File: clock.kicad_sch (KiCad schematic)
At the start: 31 parts, among them J1 USB_C_Receptacle_USB2.0_16P, J2 Conn_01x02_Pin, J3 Conn_01x02_Pin, J4 Conn_01x02_Pin, SW1 SW_Push, SW2 SW_Push, SW3 SW_Push, U1 STM32F072CBT6, U2 USBLC6-2SC6, U3 AZ1117C-3.3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

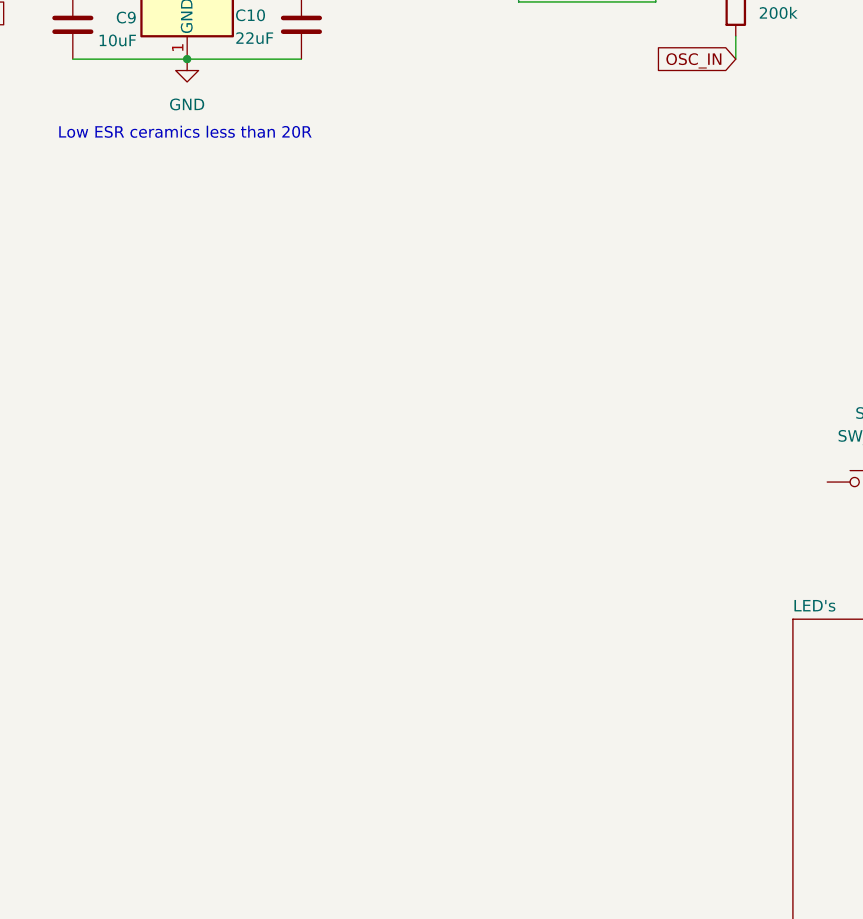
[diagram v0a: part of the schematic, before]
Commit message: started adding charging ic
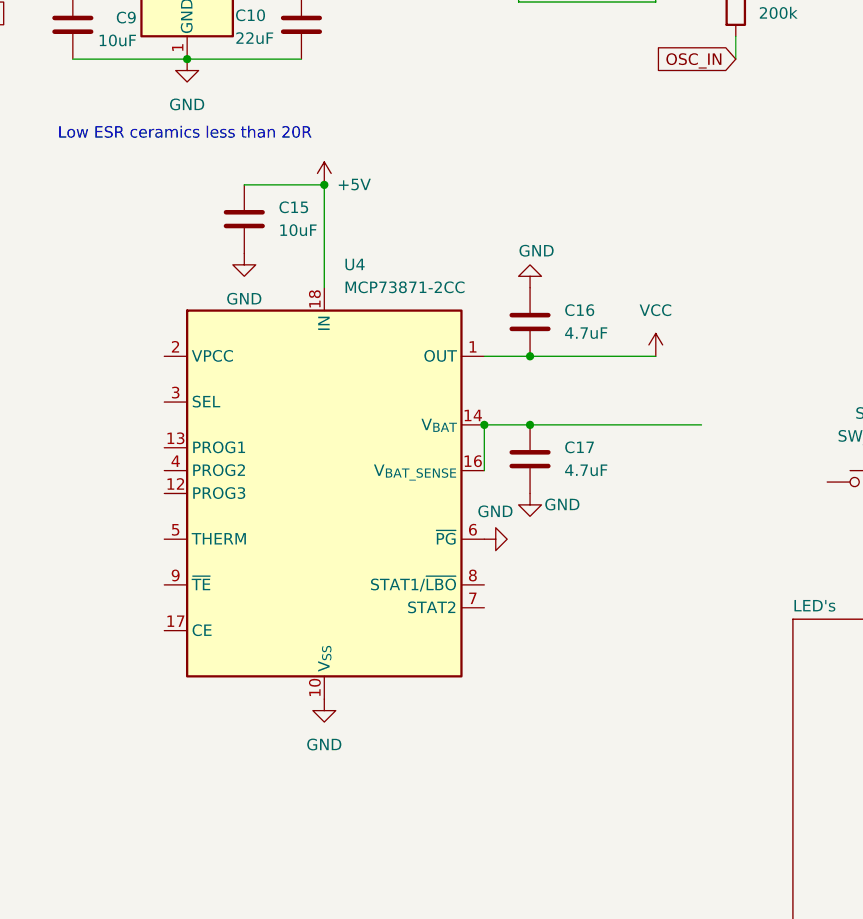
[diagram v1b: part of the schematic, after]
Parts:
- added C15: 10uF, symbol Device:C
- added C16, C17: 4.7uF, symbol Device:C
- added U4: MCP73871-2CC, Package_DFN_QFN:QFN-20-1EP_4x4mm_P0.5mm_EP2.5x2.5mm, symbol Battery_Management:MCP73871-2CC
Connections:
- net +5V: now also C15.1, U4.18 (IN), U4.19 (IN)
- net GND: now also C15.2, C16.1, C17.2, U4.10 (V_{SS}), U4.11 (V_{SS}), U4.21 (V_{SS}), U4.6 (~{PG})
- new net: C17.1, U4.14 (V_{BAT}), U4.15 (V_{BAT}), U4.16 (V_{BAT_SENSE})
- new net VCC: C16.2, U4.1 (OUT), U4.20 (OUT)

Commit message: nothing really
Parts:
- added R6, R7: 470R, symbol Device:R
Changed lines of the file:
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@@
+	)
+	(symbol
+		(lib_id "Device:R")
+		(at 162.56 107.95 90)
+		(unit 1)
+		(exclude_from_sim no)
+		(in_bom yes)
+		(on_board yes)
+		(dnp no)
+		(property "Reference" "R6"
+			(at 162.56 103.886 90)
+			(effects
+				(font
+					(size 1.27 1.27)
+				)
+			)
+		)
+		(property "Value" "470R"
+			(at 162.56 105.664 90)
+			(effects
+				(font
+					(size 1.27 1.27)
+				)
+			)
+		)
+		(property "Footprint" ""
+			(at 162.56 109.728 90)
+			(effects
+				(font
+					(size 1.27 1.27)
+				)
+				(hide yes)
+			)
+		)
+		(property "Datasheet" "~"
+			(at 162.56 107.95 0)
+			(effects
+				(font
+					(size 1.27 1.27)
+				)
+				(hide yes)
+			)
+		)
+		(property "Description" "Resistor"
+			(at 162.56 107.95 0)
+			(effects
+				(font
+					(size 1.27 1.27)
+				)
+				(hide yes)
+			)
+		)
+		(pin "1"
+		)
+		(pin "2"
+		)
+		(instances
+			(project "clock"
+				(path "/959d2641-02eb-4caa-b1c6-84a86321825f"
+					(reference "R6")
+					(unit 1)
+				)
+			)
+		)
 	)
 	(symbol
@@
 					(unit 1)
 				)
+			)
+		)
+	)
+	(symbol
+		(lib_id "Device:R")
+		(at 162.56 110.49 90)
+		(unit 1)
+		(exclude_from_sim no)
+		(in_bom yes)
+		(on_board yes)
+		(dnp no)
+		(property "Reference" "R7"
+			(at 162.56 115.062 90)
+			(effects
+				(font
+					(size 1.27 1.27)
+				)
+			)
+		)
+		(property "Value" "470R"
+			(at 162.56 113.284 90)
+			(effects
+				(font
+					(size 1.27 1.27)
+				)
+			)
+		)
+		(property "Footprint" ""
+			(at 162.56 112.268 90)
+			(effects
+				(font
+					(size 1.27 1.27)
+				)
+				(hide yes)
+			)
+		)
+		(property "Datasheet" "~"
+			(at 162.56 110.49 0)
+			(effects
+				(font
+					(size 1.27 1.27)
+				)
+				(hide yes)
+			)
+		)
+		(property "Description" "Resistor"
+			(at 162.56 110.49 0)
+			(effects
+				(font
+					(size 1.27 1.27)
+				)
+				(hide yes)
+			)
+		)
+		(pin "1"
+		)
+		(pin "2"
+		)
+		(instances
+			(project "clock"
+				(path "/959d2641-02eb-4caa-b1c6-84a86321825f"
+					(reference "R7")
+					(unit 1)
+				)

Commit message: changed resistor value
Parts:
- added R5: 1kR, symbol Device:R
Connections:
- net +5V: now also U4.4 (PROG2)
- net at U4.13 (PROG1): now also R5.2
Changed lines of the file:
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@@
 	(wire
 		(pts
+			(xy 114.3 92.71) (xy 118.11 92.71)
+		)
+		(stroke
+			(width 0)
+			(type default)
+		)
+	)
+	(wire
+		(pts
 			(xy 252.73 26.67) (xy 262.89 26.67)
 		)
@@
 	)
 	(symbol
+		(lib_id "power:+5V")
+		(at 118.11 95.25 90)
+		(unit 1)
+		(exclude_from_sim no)
+		(in_bom yes)
+		(on_board yes)
+		(dnp no)
+		(property "Reference" "#PWR027"
+			(at 121.92 95.25 0)
+			(effects
+				(font
+					(size 1.27 1.27)
+				)
+				(hide yes)
+			)
+		)
+		(property "Value" "+5V"
+			(at 112.776 95.25 90)
+			(effects
+				(font
+					(size 1.27 1.27)
+				)
+			)
+		)
+		(property "Footprint" ""
+			(at 118.11 95.25 0)
+			(effects
+				(font
+					(size 1.27 1.27)
+				)
+				(hide yes)
+			)
+		)
+		(property "Datasheet" ""
+			(at 118.11 95.25 0)
+			(effects
+				(font
+					(size 1.27 1.27)
+				)
+				(hide yes)
+			)
+		)
+		(property "Description" "Power symbol creates a global label with name \"+5V\""
+			(at 118.11 95.25 0)
+			(effects
+				(font
+					(size 1.27 1.27)
+				)
+				(hide yes)
+			)
+		)
+		(pin "1"
+		)
+		(instances
+			(project "clock"
+				(path "/959d2641-02eb-4caa-b1c6-84a86321825f"
+					(reference "#PWR027")
+					(unit 1)
+				)
+			)
+		)
+	)
+	(symbol
 		(lib_id "Device:C")
 		(at 44.45 104.14 0)
@@
 		)
 		(instances
-			(project ""
+			(project "clock"
 				(path "/959d2641-02eb-4caa-b1c6-84a86321825f"
 					(reference "#PWR028")
@@
 	)
 	(symbol
+		(lib_id "Device:R")
+		(at 110.49 92.71 90)
+		(unit 1)
+		(exclude_from_sim no)
+		(in_bom yes)
+		(on_board yes)
+		(dnp no)
+		(fields_autoplaced yes)
+		(property "Reference" "R5"
+			(at 110.49 86.36 90)
+			(effects
+				(font
+					(size 1.27 1.27)
+				)
+			)
+		)
+		(property "Value" "1kR"
+			(at 110.49 88.9 90)
+			(effects
+				(font
+					(size 1.27 1.27)
+				)
+			)
+		)
+		(property "Footprint" ""
+			(at 110.49 94.488 90)
+			(effects
+				(font
+					(size 1.27 1.27)
+				)
+				(hide yes)
+			)
+		)
+		(property "Datasheet" "~"
+			(at 110.49 92.71 0)
+			(effects
+				(font
+					(size 1.27 1.27)
+				)
+				(hide yes)
+			)
+		)
+		(property "Description" "Resistor"
+			(at 110.49 92.71 0)
+			(effects
+				(font
+					(size 1.27 1.27)
+				)
+				(hide yes)
+			)
+		)
+		(pin "2"
+		)
+		(pin "1"
+		)
+		(instances
+			(project "clock"
+				(path "/959d2641-02eb-4caa-b1c6-84a86321825f"
+					(reference "R5")
+					(unit 1)
+				)
+			)
+		)
+	)
+	(symbol
 		(lib_id "Connector:Conn_01x02_Pin")
 		(at 251.46 40.64 270)
@@
 		)
 		(instances
-			(project ""
+			(project "clock"
 				(path "/959d2641-02eb-4caa-b1c6-84a86321825f"
 					(reference "#PWR021")
@@
 		)
 		(instances
-			(project ""
+			(project "clock"
 				(path "/959d2641-02eb-4caa-b1c6-84a86321825f"
 					(reference "#PWR024")
@@
 		)
 		(instances
-			(project ""
+			(project "clock"
 				(path "/959d2641-02eb-4caa-b1c6-84a86321825f"
 					(reference "U4")
@@
 		)
 		(instances
-			(project ""
+			(project "clock"
 				(path "/959d2641-02eb-4caa-b1c6-84a86321825f"
 					(reference "C15")
@@
 		)
 		(instances
-			(project ""
+			(project "clock"
 				(path "/959d2641-02eb-4caa-b1c6-84a86321825f"
 					(reference "#PWR023")

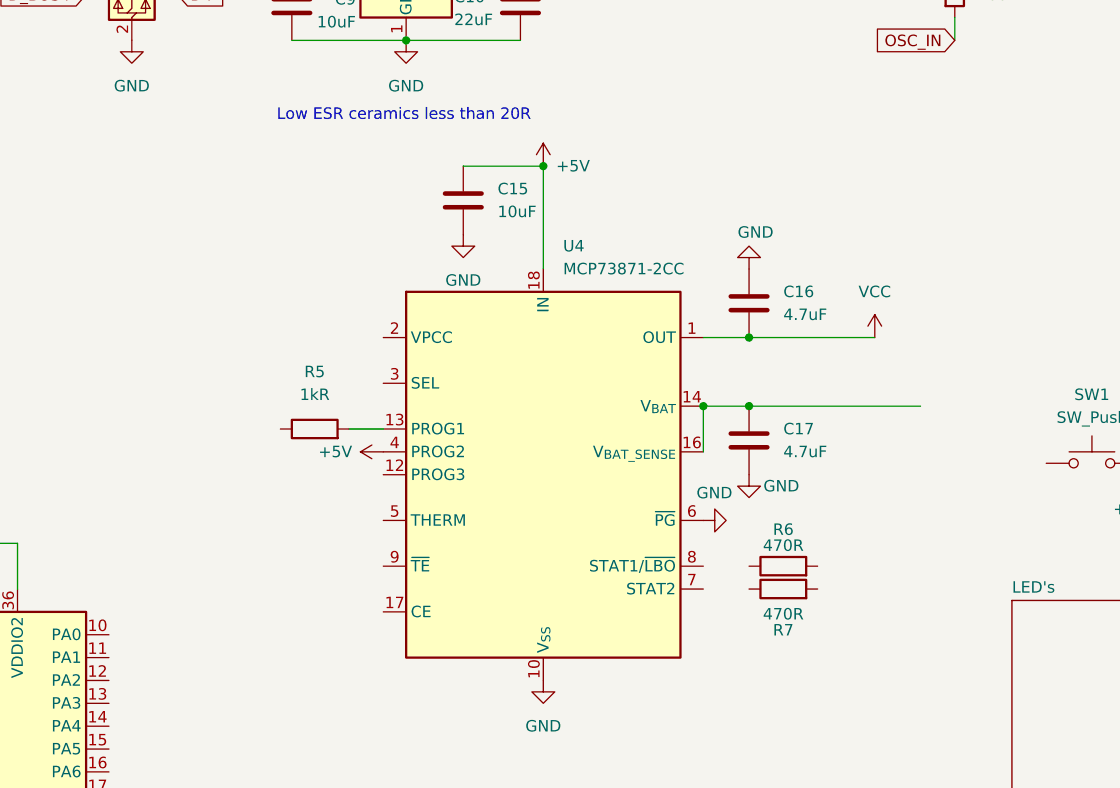
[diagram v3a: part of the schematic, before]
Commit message: most of the charging ic set up
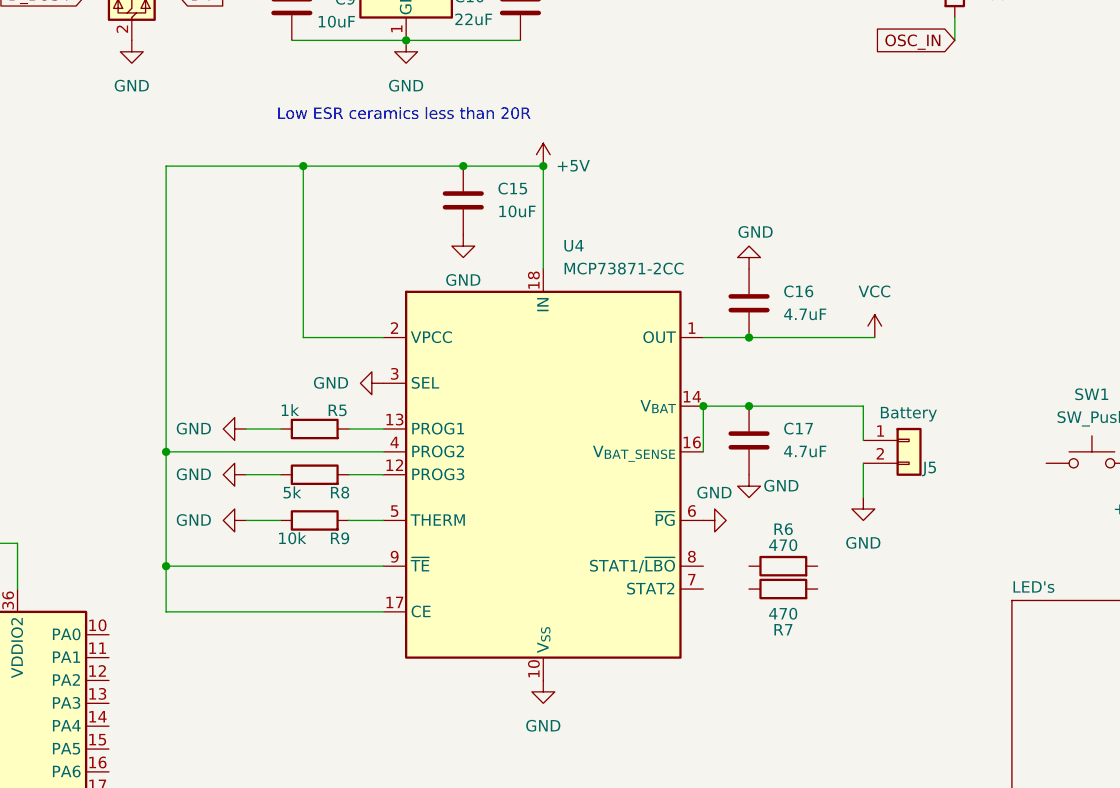
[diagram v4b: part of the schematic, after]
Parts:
- added J5: Battery, symbol Connector_Generic:Conn_01x02
- added R8: 5k, symbol Device:R
- added R9: 10k, symbol Device:R
- R5: value 1kR -> 1k
- R6, R7: value 470R -> 470
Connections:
- net +5V: now also U4.17 (CE), U4.2 (VPCC), U4.9 (~{TE})
- net GND: now also R5.1, U4.3 (SEL), J5.2 (Pin_2), R8.1, R9.1
- net at C17.1, U4.14 (V_{BAT}), U4.15 (V_{BAT})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: now also J5.1 (Pin_1)
- net at U4.12 (PROG3): now also R8.2
- net at U4.5 (THERM): now also R9.2

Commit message: litteraly nothing
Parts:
- added SW4: SW_SPDT, symbol Switch:SW_SPDT
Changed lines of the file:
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@@
+	)
+	(symbol
+		(lib_id "Switch:SW_SPDT")
+		(at 114.3 143.51 0)
+		(unit 1)
+		(exclude_from_sim no)
+		(in_bom yes)
+		(on_board yes)
+		(dnp no)
+		(fields_autoplaced yes)
+		(property "Reference" "SW4"
+			(at 114.3 134.62 0)
+			(effects
+				(font
+					(size 1.27 1.27)
+				)
+			)
+		)
+		(property "Value" "SW_SPDT"
+			(at 114.3 137.16 0)
+			(effects
+				(font
+					(size 1.27 1.27)
+				)
+			)
+		)
+		(property "Footprint" ""
+			(at 114.3 143.51 0)
+			(effects
+				(font
+					(size 1.27 1.27)
+				)
+				(hide yes)
+			)
+		)
+		(property "Datasheet" "~"
+			(at 114.3 151.13 0)
+			(effects
+				(font
+					(size 1.27 1.27)
+				)
+				(hide yes)
+			)
+		)
+		(property "Description" "Switch, single pole double throw"
+			(at 114.3 143.51 0)
+			(effects
+				(font
+					(size 1.27 1.27)
+				)
+				(hide yes)
+			)
+		)
+		(pin "2"
+		)
+		(pin "1"
+		)
+		(pin "3"
+		)
+		(instances
+			(project "clock"
+				(path "/959d2641-02eb-4caa-b1c6-84a86321825f"
+					(reference "SW4")
+					(unit 1)
+				)
+			)
+		)
 	)
 	(symbol

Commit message: m
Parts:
- added Q1: PMOS, symbol Simulation_SPICE:PMOS
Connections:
- net +5V: now also SW4.2 (B)
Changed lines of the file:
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@@
+	)
+	(symbol
+		(lib_id "power:+5V")
+		(at 109.22 143.51 90)
+		(unit 1)
+		(exclude_from_sim no)
+		(in_bom yes)
+		(on_board yes)
+		(dnp no)
+		(property "Reference" "#PWR033"
+			(at 113.03 143.51 0)
+			(effects
+				(font
+					(size 1.27 1.27)
+				)
+				(hide yes)
+			)
+		)
+		(property "Value" "+5V"
+			(at 103.378 144.018 90)
+			(effects
+				(font
+					(size 1.27 1.27)
+				)
+			)
+		)
+		(property "Footprint" ""
+			(at 109.22 143.51 0)
+			(effects
+				(font
+					(size 1.27 1.27)
+				)
+				(hide yes)
+			)
+		)
+		(property "Datasheet" ""
+			(at 109.22 143.51 0)
+			(effects
+				(font
+					(size 1.27 1.27)
+				)
+				(hide yes)
+			)
+		)
+		(property "Description" "Power symbol creates a global label with name \"+5V\""
+			(at 109.22 143.51 0)
+			(effects
+				(font
+					(size 1.27 1.27)
+				)
+				(hide yes)
+			)
+		)
+		(pin "1"
+		)
+		(instances
+			(project "clock"
+				(path "/959d2641-02eb-4caa-b1c6-84a86321825f"
+					(reference "#PWR033")
+					(unit 1)
+				)
+			)
+		)
 	)
 	(symbol
@@
 					(unit 1)
 				)
+			)
+		)
+	)
+	(symbol
+		(lib_id "Simulation_SPICE:PMOS")
+		(at 114.3 154.94 0)
+		(unit 1)
+		(exclude_from_sim no)
+		(in_bom yes)
+		(on_board yes)
+		(dnp no)
+		(fields_autoplaced yes)
+		(property "Reference" "Q1"
+			(at 120.65 153.6699 0)
+			(effects
+				(font
+					(size 1.27 1.27)
+				)
+				(justify left)
+			)
+		)
+		(property "Value" "PMOS"
+			(at 120.65 156.2099 0)
+			(effects
+				(font
+					(size 1.27 1.27)
+				)
+				(justify left)
+			)
+		)
+		(property "Footprint" ""
+			(at 119.38 152.4 0)
+			(effects
+				(font
+					(size 1.27 1.27)
+				)
+				(hide yes)
+			)
+		)
+		(property "Datasheet" "https://ngspice.sourceforge.io/docs/ngspice-html-manual/manual.xhtml#cha_MOSFETs"
+			(at 114.3 167.64 0)
+			(effects
+				(font
+					(size 1.27 1.27)
+				)
+				(hide yes)
+			)
+		)
+		(property "Description" "P-MOSFET transistor, drain/source/gate"
+			(at 114.3 154.94 0)
+			(effects
+				(font
+					(size 1.27 1.27)
+				)
+				(hide yes)
+			)
+		)
+		(property "Sim.Device" "PMOS"
+			(at 114.3 172.085 0)
+			(effects
+				(font
+					(size 1.27 1.27)
+				)
+				(hide yes)
+			)
+		)
+		(property "Sim.Type" "VDMOS"
+			(at 114.3 173.99 0)
+			(effects
+				(font
+					(size 1.27 1.27)
+				)
+				(hide yes)
+			)
+		)
+		(property "Sim.Pins" "1=D 2=G 3=S"
+			(at 114.3 170.18 0)
+			(effects
+				(font
+					(size 1.27 1.27)
+				)
+				(hide yes)
+			)
+		)
+		(pin "3"
+		)
+		(pin "2"
+		)
+		(pin "1"
+		)
+		(instances
+			(project ""
+				(path "/959d2641-02eb-4caa-b1c6-84a86321825f"
+					(reference "Q1")
+					(unit 1)
+				)

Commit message: added some r
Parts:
- added R10: 330k, symbol Device:R
- added R11: 110k, symbol Device:R
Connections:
- net +5V: now also R10.1; no longer U4.2 (VPCC)
- net GND: now also R11.1
- new net: R10.2, R11.2, U4.2 (VPCC)
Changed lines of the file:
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@@
 	)
 	(junction
+		(at 109.22 82.55)
+		(diameter 0)
+		(color 0 0 0 0)
+	)
+	(junction
 		(at 254 45.72)
 		(diameter 0)
@@
 	(wire
 		(pts
-			(xy 109.22 82.55) (xy 109.22 63.5)
+			(xy 109.22 82.55) (xy 109.22 77.47)
 		)
 		(stroke
@@
 	(wire
 		(pts
+			(xy 109.22 69.85) (xy 109.22 63.5)
+		)
+		(stroke
+			(width 0)
+			(type default)
+		)
+	)
+	(wire
+		(pts
 			(xy 262.89 26.67) (xy 262.89 27.94)
 		)
@@
 	)
 	(symbol
+		(lib_id "Device:R")
+		(at 105.41 82.55 90)
+		(unit 1)
+		(exclude_from_sim no)
+		(in_bom yes)
+		(on_board yes)
+		(dnp no)
+		(property "Reference" "R11"
+			(at 107.188 80.01 90)
+			(effects
+				(font
+					(size 1.27 1.27)
+				)
+				(justify left)
+			)
+		)
+		(property "Value" "110k"
+			(at 107.696 85.344 90)
+			(effects
+				(font
+					(size 1.27 1.27)
+				)
+				(justify left)
+			)
+		)
+		(property "Footprint" ""
+			(at 105.41 84.328 90)
+			(effects
+				(font
+					(size 1.27 1.27)
+				)
+				(hide yes)
+			)
+		)
+		(property "Datasheet" "~"
+			(at 105.41 82.55 0)
+			(effects
+				(font
+					(size 1.27 1.27)
+				)
+				(hide yes)
+			)
+		)
+		(property "Description" "Resistor"
+			(at 105.41 82.55 0)
+			(effects
+				(font
+					(size 1.27 1.27)
+				)
+				(hide yes)
+			)
+		)
+		(pin "1"
+		)
+		(pin "2"
+		)
+		(instances
+			(project "clock"
+				(path "/959d2641-02eb-4caa-b1c6-84a86321825f"
+					(reference "R11")
+					(unit 1)
+				)
+			)
+		)
+	)
+	(symbol
 		(lib_id "power:GND")
 		(at 102.87 102.87 270)
@@
 	(symbol
 		(lib_id "power:GND")
+		(at 101.6 82.55 270)
+		(unit 1)
+		(exclude_from_sim no)
+		(in_bom yes)
+		(on_board yes)
+		(dnp no)
+		(property "Reference" "#PWR034"
+			(at 95.25 82.55 0)
+			(effects
+				(font
+					(size 1.27 1.27)
+				)
+				(hide yes)
+			)
+		)
+		(property "Value" "GND"
+			(at 98.806 82.55 90)
+			(effects
+				(font
+					(size 1.27 1.27)
+				)
+				(justify right)
+			)
+		)
+		(property "Footprint" ""
+			(at 101.6 82.55 0)
+			(effects
+				(font
+					(size 1.27 1.27)
+				)
+				(hide yes)
+			)
+		)
+		(property "Datasheet" ""
+			(at 101.6 82.55 0)
+			(effects
+				(font
+					(size 1.27 1.27)
+				)
+				(hide yes)
+			)
+		)
+		(property "Description" "Power symbol creates a global label with name \"GND\" , ground"
+			(at 101.6 82.55 0)
+			(effects
+				(font
+					(size 1.27 1.27)
+				)
+				(hide yes)
+			)
+		)
+		(pin "1"
+		)
+		(instances
+			(project "clock"
+				(path "/959d2641-02eb-4caa-b1c6-84a86321825f"
+					(reference "#PWR034")
+					(unit 1)
+				)
+			)
+		)
+	)
+	(symbol
+		(lib_id "power:GND")
 		(at 118.11 87.63 270)
 		(unit 1)
@@
 					(unit 1)
 				)
+			)
+		)
+	)
+	(symbol
+		(lib_id "Device:R")
+		(at 109.22 73.66 0)
+		(unit 1)
+		(exclude_from_sim no)
+		(in_bom yes)
+		(on_board yes)
+		(dnp no)
+		(property "Reference" "R10"
+			(at 111.76 72.3899 0)
+			(effects
+				(font
+					(size 1.27 1.27)
+				)
+				(justify left)
+			)
+		)
+		(property "Value" "330k"
+			(at 111.76 74.9299 0)
+			(effects
+				(font
+					(size 1.27 1.27)
+				)
+				(justify left)
+			)
+		)
+		(property "Footprint" ""
+			(at 107.442 73.66 90)
+			(effects
+				(font
+					(size 1.27 1.27)
+				)
+				(hide yes)
+			)
+		)
+		(property "Datasheet" "~"
+			(at 109.22 73.66 0)
+			(effects
+				(font
+					(size 1.27 1.27)
+				)
+				(hide yes)
+			)
+		)
+		(property "Description" "Resistor"
+			(at 109.22 73.66 0)
+			(effects
+				(font
+					(size 1.27 1.27)
+				)
+				(hide yes)
+			)
+		)
+		(pin "1"
+		)
+		(pin "2"
+		)
+		(instances
+			(project ""
+				(path "/959d2641-02eb-4caa-b1c6-84a86321825f"
+					(reference "R10")
+					(unit 1)
+				)

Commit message: new st cube ide files
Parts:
- removed Q1: PMOS, symbol Simulation_SPICE:PMOS
- removed SW4: SW_SPDT, symbol Switch:SW_SPDT
- added R12: 470, symbol Device:R
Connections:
- net +5V: now also R6.1, R7.1, R12.1
- net GND: no longer U4.6 (~{PG})
- net at R6.2: now also U4.7 (STAT2)
- net at R7.2: now also U4.8 (STAT1/~{LBO})
- new net: R12.2, U4.6 (~{PG})
- no-connect marks 0 -> 6
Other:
- moved on the sheet: R6, R7
